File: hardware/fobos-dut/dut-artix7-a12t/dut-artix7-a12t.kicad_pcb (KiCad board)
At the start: 4 copper layers, 88.9 x 76.2 mm, 181 parts, among them J1 Target, J2 Pmod 2x6, J3 575-8, J4 Glitch, J6 Measure, J7 0878321420, J8 575-8, J9 Measure, Q1 FDS9435A, Q2 MBT3904DW1, Q3 FDV301N, Q4 BSS138, Q5 BSS138, Q6 BSS138, Q7 BSS138, SW1 SW_DIP_x03, SW2 SW_DIP_x03, U1 XC7A12T-CSG325, U2 SP3003-04ATG, U3 SP3003-04ATG, U4 SP3003-04ATG, U5 INA225, U6 BGA2801, U7 TS3A5018DBQR, U8 LTC3569EFE#PBF, U9 IS25LP256D-JMLE

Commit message: ARTIX 7 DUT Layout is 80% done
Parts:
- added J5: Conn_01x02, Connector_Molex:Molex_KK-254_AE-6410-02A_1x02_P2.54mm_Vertical, F.Cu at (27.4, 12.7)
- C37: moved to B.Cu
- C38: footprint Resistor_SMD:R_0805_2012Metric_Pad1.20x1.40mm_HandSolder -> Resistor_SMD:R_0402_1005Metric_Pad0.72x0.64mm_HandSolder; moved to B.Cu
- R27, R28, R29, R30, R7, R9: moved to F.Cu
- moved U6 78.8 mm to (-8.89, 14.2)
- moved C12 76.5 mm to (-12.4, 20.6)
- moved C13 76.5 mm to (-12.5, 24.4)
- moved C14 76.5 mm to (-9.89, 8.13)
- moved C15 76.5 mm to (-12.4, 16.8)
- moved L2 76.5 mm to (-12.7, 13.0)
- moved R30 42.4 mm to (19.3, 58.2), turned to 270 degrees
- moved U5 32.2 mm to (48.3, 9.90), turned to 180 degrees
- moved R29 28.4 mm to (17.3, 58.2), turned to 270 degrees
- moved TP7 27.0 mm to (35.6, 55.9)
- moved R27 25.1 mm to (81.3, 31.7), turned to 180 degrees
- moved R67 24.4 mm to (23.1, 53.8)
- moved TP3 23.6 mm to (13.2, 63.5)
- moved C24 22.3 mm to (53.9, 9.90), turned to 270 degrees
- moved C17 15.0 mm to (10.2, 30.5), turned to 270 degrees
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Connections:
- Q4 pad 1: Net-(Q4-Pad1) -> USER_LED_1
- Q5 pad 1: Net-(Q5-Pad1) -> USER_LED_2
- Q6 pad 1: Net-(Q6-Pad1) -> USER_LED_4
- Q7 pad 1: Net-(Q7-Pad1) -> USER_LED_3
- R60 pad 2: Net-(Q4-Pad1) -> USER_LED_1
- R61 pad 2: Net-(Q5-Pad1) -> USER_LED_2
- R62 pad 2: Net-(Q7-Pad1) -> USER_LED_3
- R64 pad 2: Net-(R64-Pad2) -> USER_BTN_1
- R66 pad 2: Net-(R66-Pad2) -> USER_BTN_2
- R68 pad 2: Net-(Q6-Pad1) -> USER_LED_4
- U1 pad J14: JA3 -> Net-(U1-PadJ14)
- U1 pad J15: JA1 -> Net-(U1-PadJ15)
- U1 pad J16: JA7 -> Net-(U1-PadJ16)
- U1 pad K15: JA9 -> Net-(U1-PadK15)
- U1 pad K17: JA2 -> Net-(U1-PadK17)
- U1 pad L18: JA8 -> Net-(U1-PadL18)
- U1 pad M16: JA4 -> Net-(U1-PadM16)
- U1 pad M17: JA10 -> Net-(U1-PadM17)
- U1 pad R18: Net-(U1-PadR18) -> JA2
- U1 pad T17: Net-(U1-PadT17) -> JA3
- U1 pad T18: Net-(U1-PadT18) -> JA1
- U1 pad U14: Net-(U1-PadU14) -> USER_LED_4
- U1 pad U15: Net-(U1-PadU15) -> JA10
- U1 pad U16: Net-(U1-PadU16) -> JA8
- U1 pad U17: Net-(U1-PadU17) -> JA4
- U1 pad U9: Net-(U1-PadU9) -> USER_BTN_1
- U1 pad V12: Net-(U1-PadV12) -> USER_LED_1
- U1 pad V13: Net-(U1-PadV13) -> USER_LED_2
- U1 pad V14: Net-(U1-PadV14) -> USER_LED_3
- U1 pad V16: Net-(U1-PadV16) -> JA9
- U1 pad V17: Net-(U1-PadV17) -> JA7
- U1 pad V9: Net-(U1-PadV9) -> USER_BTN_2
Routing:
- net FC_3V3: track 10.1 -> 263.0 mm, vias 4 -> 13
- net VCORE_CURRENT_GAIN_0: track 0.00 -> 94.2 mm, vias 0 -> 3
- net GND: track 100.8 -> 193.6 mm, vias 109 -> 152
- net VCORE_CURRENT_GAIN_1: track 0.00 -> 90.4 mm, vias 0 -> 3
- net +1V0: track 0.00 -> 52.6 mm, vias 0 -> 3
- net SW_PROGRAM_B: track 0.57 -> 48.1 mm, vias 1 -> 0
- net USER_BTN_2: track 0.00 -> 46.7 mm, vias 0 -> 1
- net +5V: track 0.00 -> 43.8 mm, vias 0 -> 8
- net JA10: track 0.00 -> 40.3 mm
- net FC_5V: track 0.00 -> 39.9 mm, vias 0 -> 2
- net USER_LED_4: track 0.00 -> 39.6 mm
- net Net-(R27-Pad1): track 0.00 -> 38.5 mm, vias 0 -> 2
- net JA9: track 0.00 -> 36.6 mm
- net JA8: track 0.00 -> 35.1 mm
- net USER_LED_3: track 0.00 -> 33.6 mm
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- added copper zone on In1.Cu, net (none)
- added copper zone on F.Cu, net +1V0
- added copper zone on B.Cu, net +1V8
- added copper zone on F.Cu, net +1V8
- added copper zone on F.Cu, net +3V3
- added copper zone on In2.Cu, net +3V3
- added copper zone on B.Cu, net +5V
- added copper zone on F.Cu, net +5V
- added copper zone on In2.Cu, net +5V
- added copper zone on B.Cu, net FC_5V
- added copper zone on In2.Cu, net FC_5V
- added copper zone on B.Cu, net GND
- added copper zone on B.Cu, net Net-(C5-Pad1)
- added copper zone on B.Cu, net Net-(C7-Pad1)
- added copper zone on B.Cu, net Net-(F1-Pad2)
- added copper zone on In2.Cu, net Net-(J5-Pad1)
- added copper zone on F.Cu, net Net-(JP2-Pad2)
- added copper zone on In2.Cu, net Net-(JP2-Pad2)
- added copper zone on F.Cu, net Net-(L3-Pad1)
- added copper zone on F.Cu, net Net-(L4-Pad1)
- added copper zone on F.Cu, net VCCINT
- added copper zone on In2.Cu, net VCCINT
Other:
- net class Default: clearance 0.2 -> 0.127
- rule trace_clearance: 0.2 -> 0.127
- board text added: "Glitch"
- board text added: "Measure"
- board text added: "Measure Current"

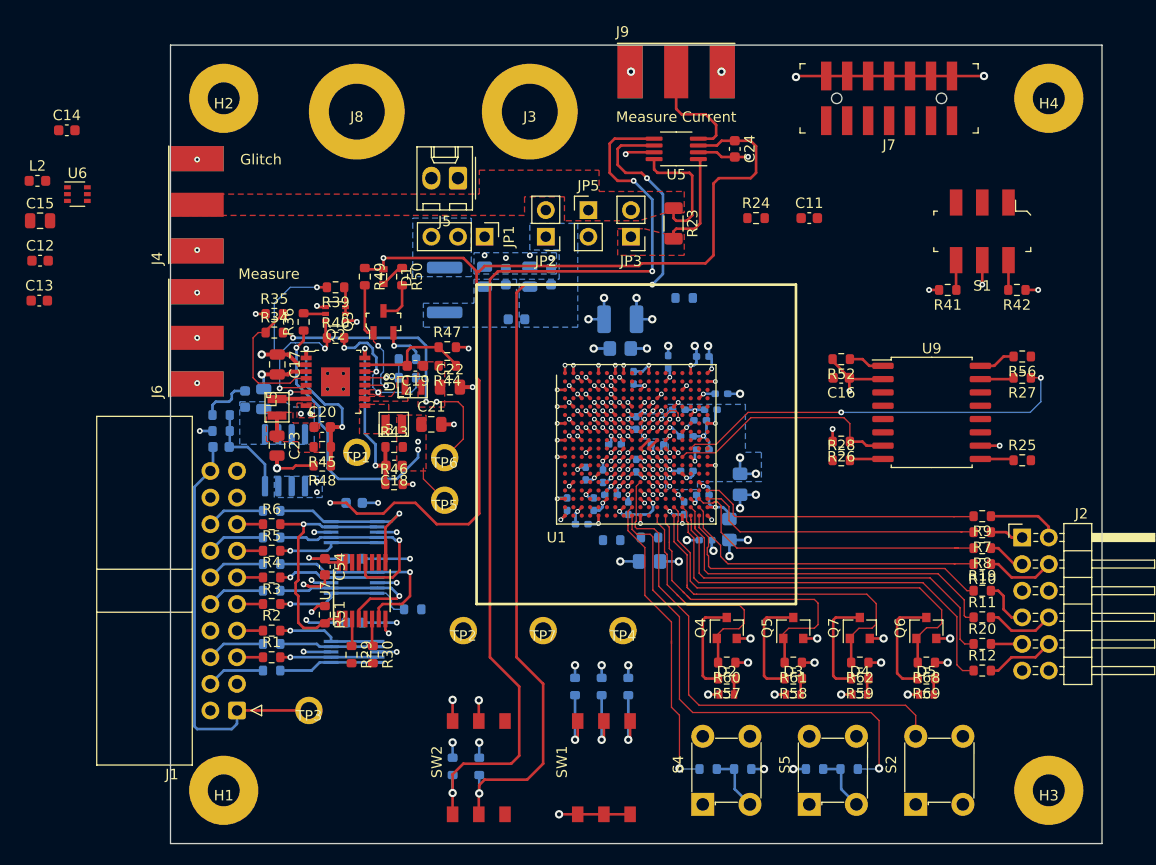
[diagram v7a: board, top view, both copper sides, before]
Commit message: Completed layout of the Artix 7 DUT Board
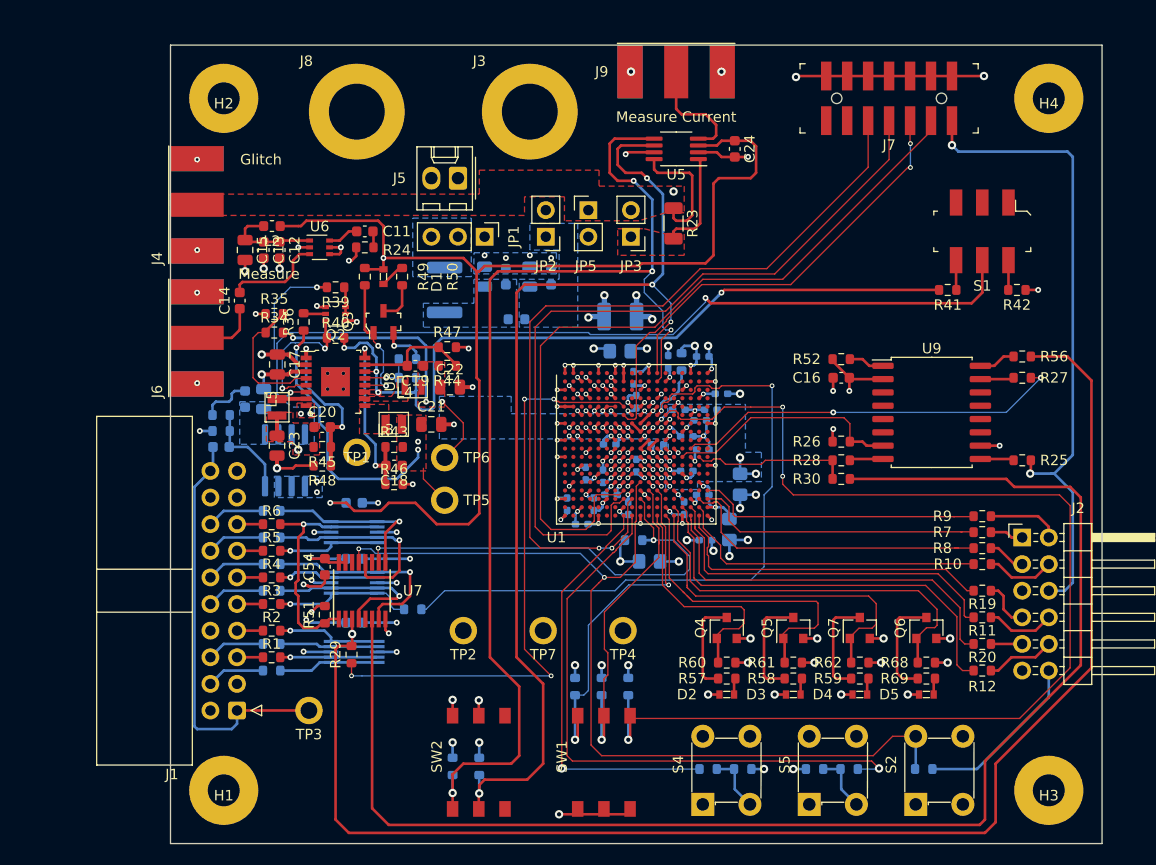
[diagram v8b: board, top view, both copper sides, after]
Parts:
- moved R30 47.7 mm to (64.0, 41.4), turned to 180 degrees
- moved C11 42.4 mm to (18.5, 17.8)
- moved R24 37.4 mm to (18.5, 19.3), turned to 180 degrees
- moved R54 36.9 mm to (71.9, 69.1), turned to 0 degrees
- moved U6 23.7 mm to (14.2, 19.3)
- moved C14 23.2 mm to (6.61, 24.4), turned to 90 degrees
- moved C12 22.9 mm to (10.4, 19.6), turned to 270 degrees
- moved L2 22.8 mm to (9.68, 17.3), turned to 180 degrees
- moved C13 22.0 mm to (8.89, 19.6), turned to 270 degrees
- moved C15 19.8 mm to (7.12, 19.6), turned to 270 degrees
- moved R53 6.10 mm to (48.8, 30.2), turned to 90 degrees
- moved C29 2.03 mm to (44.5, 34.0)
- moved R55 1.54 mm to (44.2, 47.2), turned to 180 degrees
- moved SW1 0.51 mm to (38.9, 72.9)
- moved SW2 0.51 mm to (26.9, 72.9)
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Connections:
- U1 pad A12: Net-(U1-PadA12) -> VCORE_CURRENT_GAIN_1
- U1 pad B12: Net-(U1-PadB12) -> VCORE_CURRENT_GAIN_0
- U1 pad U9: USER_BTN_1 -> Net-(U1-PadU9)
- U1 pad V8: Net-(U1-PadV8) -> USER_BTN_1
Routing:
- net +3V3: track 55.2 -> 252.8 mm, vias 30 -> 32
- net SW_CLK: track 2.59 -> 137.1 mm, vias 0 -> 1
- net SW_DIN: track 2.60 -> 134.7 mm
- net Net-(R33-Pad2): track 8.15 -> 113.9 mm, vias 2 -> 3
- net ON_OFF: track 3.85 -> 81.1 mm
- net Net-(J7-Pad10): track 0.00 -> 77.2 mm, vias 0 -> 2
- net Net-(J7-Pad8): track 0.00 -> 74.8 mm
- net Net-(J7-Pad4): track 0.00 -> 74.5 mm
- net SW_DONE: track 0.57 -> 70.0 mm, vias 1 -> 2
- net VCCINT: track 33.4 -> 102.1 mm
- net +5V: track 43.8 -> 102.4 mm
- net Net-(R29-Pad2): track 0.57 -> 57.5 mm, vias 1 -> 4
- net Net-(J7-Pad6): track 0.00 -> 46.1 mm, vias 0 -> 2
- net SW_INIT_B: track 0.57 -> 43.2 mm, vias 1 -> 2
- net SW_PROGRAM_B: track 48.1 -> 89.1 mm, vias 0 -> 2
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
